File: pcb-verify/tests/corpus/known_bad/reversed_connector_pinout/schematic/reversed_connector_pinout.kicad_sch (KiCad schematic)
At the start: 4 parts, among them J1 EXAMPLE-CONN-2P, U1 EXAMPLE-LDO-3V3

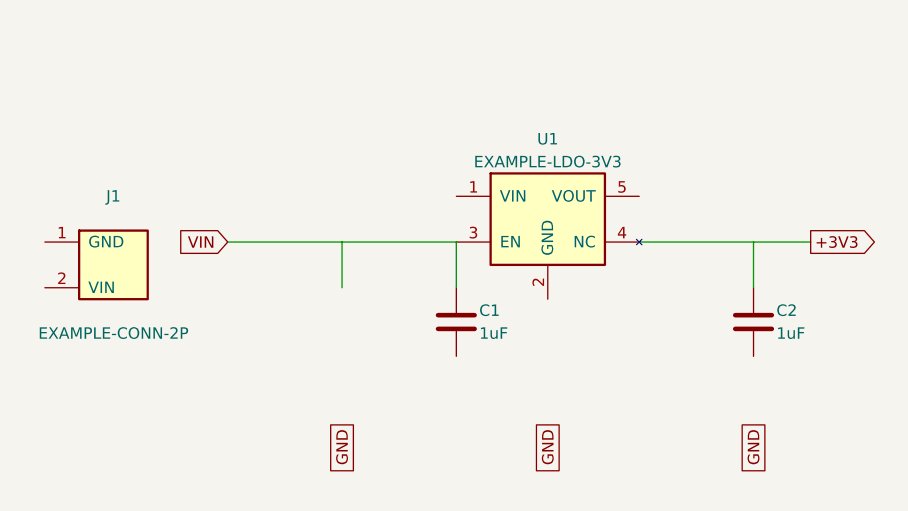
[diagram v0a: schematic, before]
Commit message: Verify corpus fixtures against real KiCad, closing the circularity
Installed kicad-cli 7.0.11 and used it to check the fixtures. It rejected all
four schematics: they were written in the KiCad 8 format (version 20231120),
which KiCad reads forward but not backward. Retargeted every fixture to the
format kicad-cli actually accepts and validated each one.

Two latent defects the fixtures had been hiding
- KiCad derives connectivity from wire endpoints, so a pin part-way along a
  segment does not connect even with a junction drawn on it. The known-good
  fixture loaded cleanly while its netlist put every pin on its own unconnected
  net. Wires are now split at every connection point and the intended circuit
  is asserted: VIN feeds the LDO input, its input capacitor and EN; +3V3 reaches
  the output capacitor from pin 5; GND ties all four returns.
- A no_connect-type pin never joins a net, so the earlier attempt to wire the
  regulated output had silently landed on the unbonded pin 4.
Pin coordinates were determined empirically by probing with uniquely-named
labels rather than assumed.

KiCad as the oracle
- New pcbv.kicad.cli wrapper. kicad-cli 7 exits 0 even after printing "Failed
  to load schematic file", so the wrapper inspects output text and the produced
  file instead of trusting exit status.
- 22 tests compare our readers against KiCad itself: same components, same pin
  numbers, names and electrical types. Without this a self-consistently wrong
  reader would make CHK-PIN-MAP compare against something the board never uses.
- Tests assert the known-good netlist is the intended circuit and that each
  known-bad fixture still carries a live defect, so a broken injection fails
  loudly rather than passing while testing nothing.
- Absent kicad-cli they skip with an explicit "UNVERIFIED" message, and CI
  fails the job if they skip there.

Symbol and footprint libraries are now KiCad's own canonical output via sym/fp
upgrade, so the committed files are the referen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
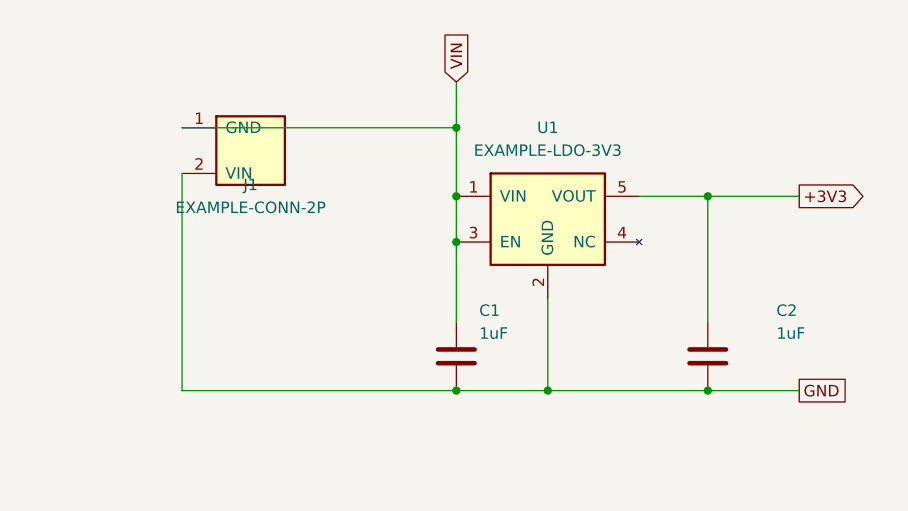
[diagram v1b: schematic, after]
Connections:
- net +3V3: now also C2.1, U1.5 (VOUT); no longer U1.4 (NC)
- net GND: now also C1.2, C2.2, J1.2 (VIN), U1.2 (GND)
- net VIN: now also J1.1 (GND), U1.1 (VIN)
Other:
- moved on the sheet: C1, C2, J1

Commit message: Verify the corpus against KiCad 10.0.5, built from source
Every packaged route to KiCad 10 is denied by this environment's egress policy
(kicad.org, downloads.kicad.org, ppa.launchpadcontent.net, Flathub, Snapcraft,
Anaconda), and no Ubuntu suite carries it -- 26.10 devel still ships 9.0.8.
GitLab is permitted, so 10.0.5 was built from source (tag 10.0.5, commit
18fb9289) and the whole corpus re-verified against it. On a machine that can
reach the PPA this is a one-line install and unnecessary.

Two real defects the newer toolchain exposed
- Netlist parsing was regex-based and assumed KiCad 7's line shape. KiCad 10
  pretty-prints every element on its own line, so all four oracle comparisons
  silently returned nothing -- which looks identical to a design with no
  components. Replaced with the project's own s-expression reader, which is
  format-agnostic and removes the whole class of fragility.
- ERC reported power_pin_not_driven on VIN and GND: the corpus header's
  contacts are passive, so nothing declared a power source. Added PWR_FLAG
  symbols, which is honest here since VIN genuinely arrives from off-board.
  Their #FLG references are skipped by the schematic reader and never reach the
  checks. All four fixtures are now ERC-error-free.

What ERC proved, now asserted as a test
ERC reports zero errors on all three deliberately broken designs. A regulator
output on an unbonded pad, a package with transposed pin numbering, a power
connector wired backwards -- none are visible to it, because ERC knows pin
electrical types and connectivity and never what the datasheet says. That is
the empirical case for this project, and it is now a test rather than a claim.

Build note for anyone repeating this: KiCad 10 on Ubuntu 24.04 needs
libpoppler-glib-dev, which cmake does not catch -- configuration succeeds with
poppler core and cpp alone, then compilation fails ~190 files in. OCC and
ngspice are unconditionally required with no option to build without them.

Fixtures s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
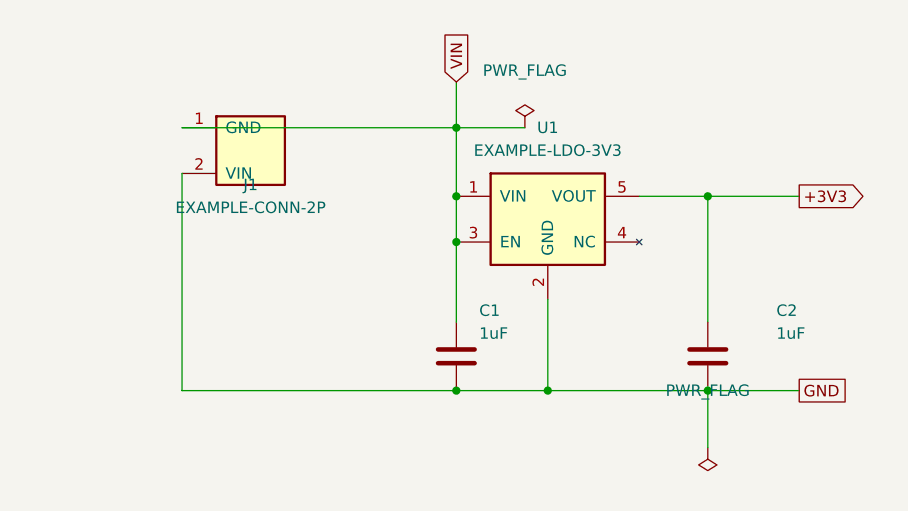
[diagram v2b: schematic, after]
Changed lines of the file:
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@@
+    (stroke (width 0) (type default))
+  )
+  (wire (pts (xy 88.9 63.5) (xy 96.52 63.5))
+    (stroke (width 0) (type default))
+  )
+  (wire (pts (xy 116.84 92.71) (xy 116.84 99.06))
     (stroke (width 0) (type default))
   )
@@
         )
       )
+    )
+  )
+  (symbol (lib_id "pcbv_example:PWR_FLAG") (at 96.52 63.5 0) (unit 1)
+    (in_bom no) (on_board yes) (dnp no) (fields_autoplaced)
+    (property "Reference" "#FLG01" (at 96.52 59.69 0)
+      (effects (font (size 1.27 1.27)) hide)
+    )
+    (property "Value" "PWR_FLAG" (at 96.52 57.15 0)
+      (effects (font (size 1.27 1.27)))
+    )
+    (property "Footprint" "" (at 96.52 63.5 0)
+      (effects (font (size 1.27 1.27)) hide)
+    )
+    (property "Datasheet" "" (at 96.52 63.5 0)
+      (effects (font (size 1.27 1.27)) hide)
+    )
+    (pin "1")
+    (instances
+      (project "minimal_ldo"
+        (path "/b1000000-0000-4000-8000-000000000001"
+          (reference "#FLG01") (unit 1)
+        )
+      )
+    )
+  )
+  (symbol (lib_id "pcbv_example:PWR_FLAG") (at 116.84 99.06 180) (unit 1)
+    (in_bom no) (on_board yes) (dnp no) (fields_autoplaced)
+    (property "Reference" "#FLG02" (at 116.84 95.25 0)
+      (effects (font (size 1.27 1.27)) hide)
+    )
+    (property "Value" "PWR_FLAG" (at 116.84 92.71000000000001 0)
+      (effects (font (size 1.27 1.27)))
+    )
+    (property "Footprint" "" (at 116.84 99.06 0)
+      (effects (font (size 1.27 1.27)) hide)
+    )
+    (property "Datasheet" "" (at 116.84 99.06 0)
+      (effects (font (size 1.27 1.27)) hide)
+    )
+    (pin "1")
+    (instances
+      (project "minimal_ldo"
+        (path "/b1000000-0000-4000-8000-000000000001"
+          (reference "#FLG02") (unit 1)
+        )
+      )
